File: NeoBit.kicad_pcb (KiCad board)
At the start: 2 copper layers, 77.5 x 45.7 mm, 22 parts, among them J1 AudioJack3_Ground, J2 Barrel_Jack_MountingPin, J3 Qwiic, J4 DotStars, J5 microbit_edge_connector, J6 NeoPixels, U1 74AHCT125, U2 MCP1702-3302E_TO92, U3 MCP1702-5002E_TO92

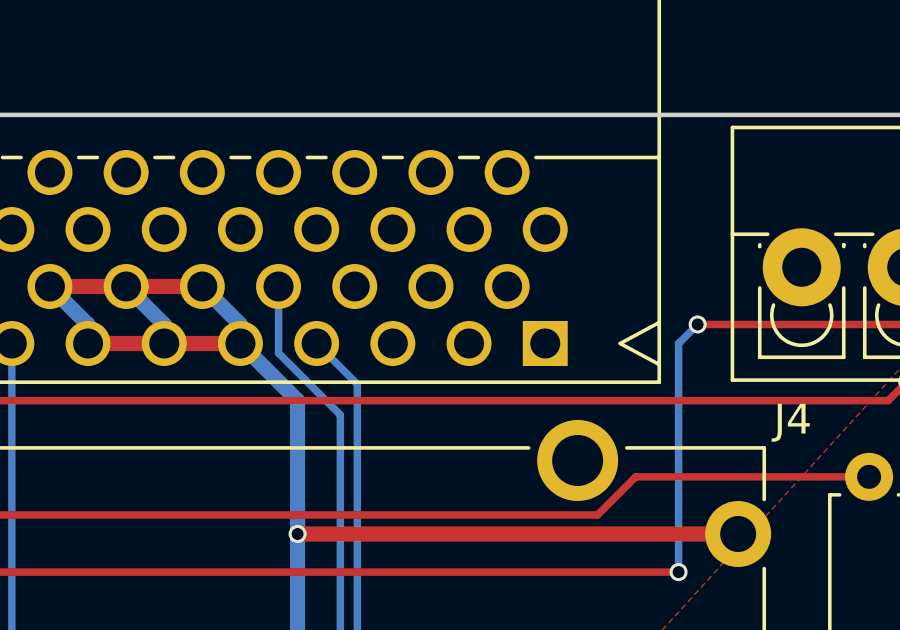
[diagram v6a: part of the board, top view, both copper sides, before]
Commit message: Filled zones; passed DRC.
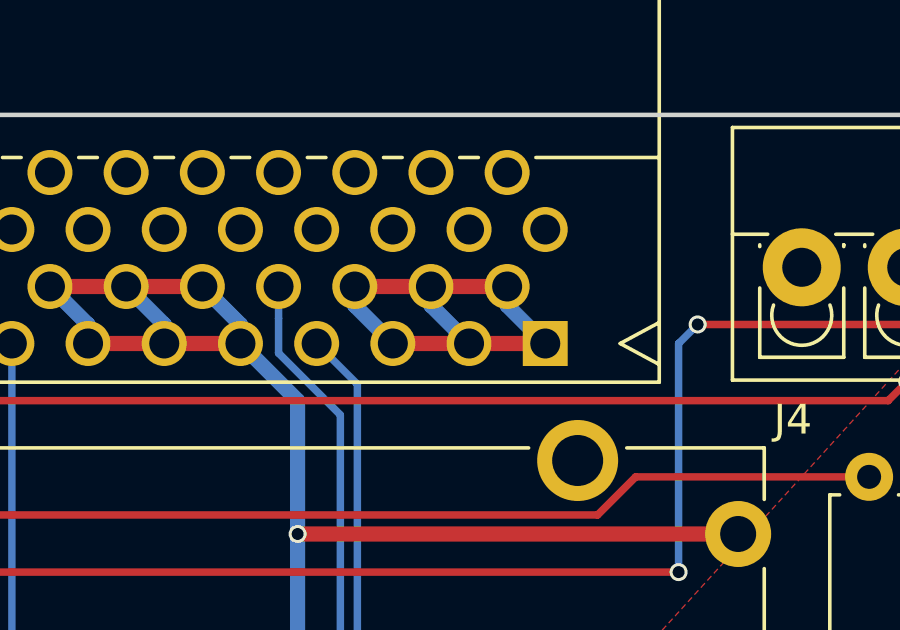
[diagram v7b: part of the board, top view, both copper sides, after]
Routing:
- net GND: track 0.00 -> 17.4 mm
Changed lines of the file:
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@@
   (general
     (links 81)
-    (no_connects 46)
+    (no_connects 0)
     (area 118.669999 83.744999 186.130001 129.615001)
     (thickness 1.6)
     (drawings 14)
-    (tracks 184)
+    (tracks 194)
     (zones 0)
     (modules 22)
@@
   )
   (setup
-    (last_trace_width 0.25)
+    (last_trace_width 0.508)
     (user_trace_width 0.508)
     (user_trace_width 1.016)
@@
   (segment (start 131.268001 114.770001) (end 131.445 114.947) (width 0.508) (layer F.Cu) (net 1))
   (segment (start 131.445 114.947) (end 131.445 116.205) (width 0.508) (layer F.Cu) (net 1))
+  (segment (start 170.18 91.44) (end 172.72 91.44) (width 0.508) (layer F.Cu) (net 2))
+  (segment (start 167.64 91.44) (end 170.18 91.44) (width 0.508) (layer F.Cu) (net 2))
+  (segment (start 168.91 89.54) (end 171.45 89.54) (width 0.508) (layer F.Cu) (net 2))
+  (segment (start 166.37 89.54) (end 168.91 89.54) (width 0.508) (layer F.Cu) (net 2))
+  (segment (start 171.45 89.54) (end 171.45 90.17) (width 0.508) (layer B.Cu) (net 2))
+  (segment (start 171.45 90.17) (end 172.72 91.44) (width 0.508) (layer B.Cu) (net 2))
+  (segment (start 168.91 89.54) (end 168.91 90.17) (width 0.508) (layer B.Cu) (net 2))
+  (segment (start 168.91 90.17) (end 170.18 91.44) (width 0.508) (layer B.Cu) (net 2))
+  (segment (start 166.37 89.54) (end 166.37 90.17) (width 0.508) (layer B.Cu) (net 2))
+  (segment (start 166.37 90.17) (end 167.64 91.44) (width 0.508) (layer B.Cu) (net 2))
   (segment (start 154.305 111.125) (end 154.305 109.855) (width 0.508) (layer B.Cu) (net 3))
   (segment (start 154.305 109.855) (end 156.845 107.315) (width 0.508) (layer B.Cu) (net 3))

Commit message: Start moving some silkscreen around.
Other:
- board text added: "+V"
- board text added: "2018-09-22 https://github.com/ppelleti/NeoBit designed by Patrick Pelletier"
- board text added: "5-12VDC IN"
- board text removed: "2018-09-03 https://github.com/ppelleti/NeoBit designed by Patrick Pelletier"
- board text removed: "5V"
- board text removed: "5VDC IN"
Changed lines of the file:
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@@
     (34 B.Paste user)
     (35 F.Paste user)
-    (36 B.SilkS user hide)
+    (36 B.SilkS user)
     (37 F.SilkS user)
     (38 B.Mask user)
@@
   (gr_line (start 121.285 129.54) (end 193.675 129.54) (angle 90) (layer Edge.Cuts) (width 0.15))
   (gr_line (start 121.285 83.82) (end 193.675 83.82) (angle 90) (layer Edge.Cuts) (width 0.15))
-  (gr_text NeoPixels (at 185 89.5 90) (layer B.SilkS)
+  (gr_text NeoPixels (at 187.96 99.695 90) (layer B.SilkS)
     (effects (font (size 1 1) (thickness 0.2)) (justify mirror))
   )
-  (gr_text "5VDC IN" (at 184.785 111.76 90) (layer B.SilkS)
+  (gr_text "5-12VDC IN" (at 194.945 122.555 90) (layer B.SilkS)
     (effects (font (size 1 1) (thickness 0.2)) (justify mirror))
   )
-  (gr_text DATA (at 180.5 91.5) (layer B.SilkS)
+  (gr_text DATA (at 192.405 100.33) (layer B.SilkS)
     (effects (font (size 1 1) (thickness 0.2)) (justify right mirror))
   )
-  (gr_text GND (at 180.5 89.5) (layer B.SilkS)
+  (gr_text GND (at 192.405 96.52) (layer B.SilkS)
     (effects (font (size 1 1) (thickness 0.2)) (justify right mirror))
   )
-  (gr_text 5V (at 180.5 87.5) (layer B.SilkS)
+  (gr_text +V (at 192.405 103.505) (layer B.SilkS)
     (effects (font (size 1 1) (thickness 0.2)) (justify right mirror))
   )
-  (gr_text "2018-09-03\nhttps://github.com/ppelleti/NeoBit\ndesigned by Patrick Pelletier" (at 154.94 99.06) (layer B.SilkS)
+  (gr_text "2018-09-22\nhttps://github.com/ppelleti/NeoBit\ndesigned by Patrick Pelletier" (at 154.94 99.06) (layer B.SilkS)
     (effects (font (size 1.5 1.5) (thickness 0.3)) (justify mirror))
   )
